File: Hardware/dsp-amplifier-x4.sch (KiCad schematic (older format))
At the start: 65 parts, among them J1 USBi, J2 EXT, J3 Raspberry_Pi_2_3, J4 Screw_Terminal_01x02, J5 Screw_Terminal_01x02, J6 Screw_Terminal_01x02, J7 Screw_Terminal_01x02, P1 Conn_WallPlug, Q1 STD2805, U1 ADAU1452, U2 TSOP583xx

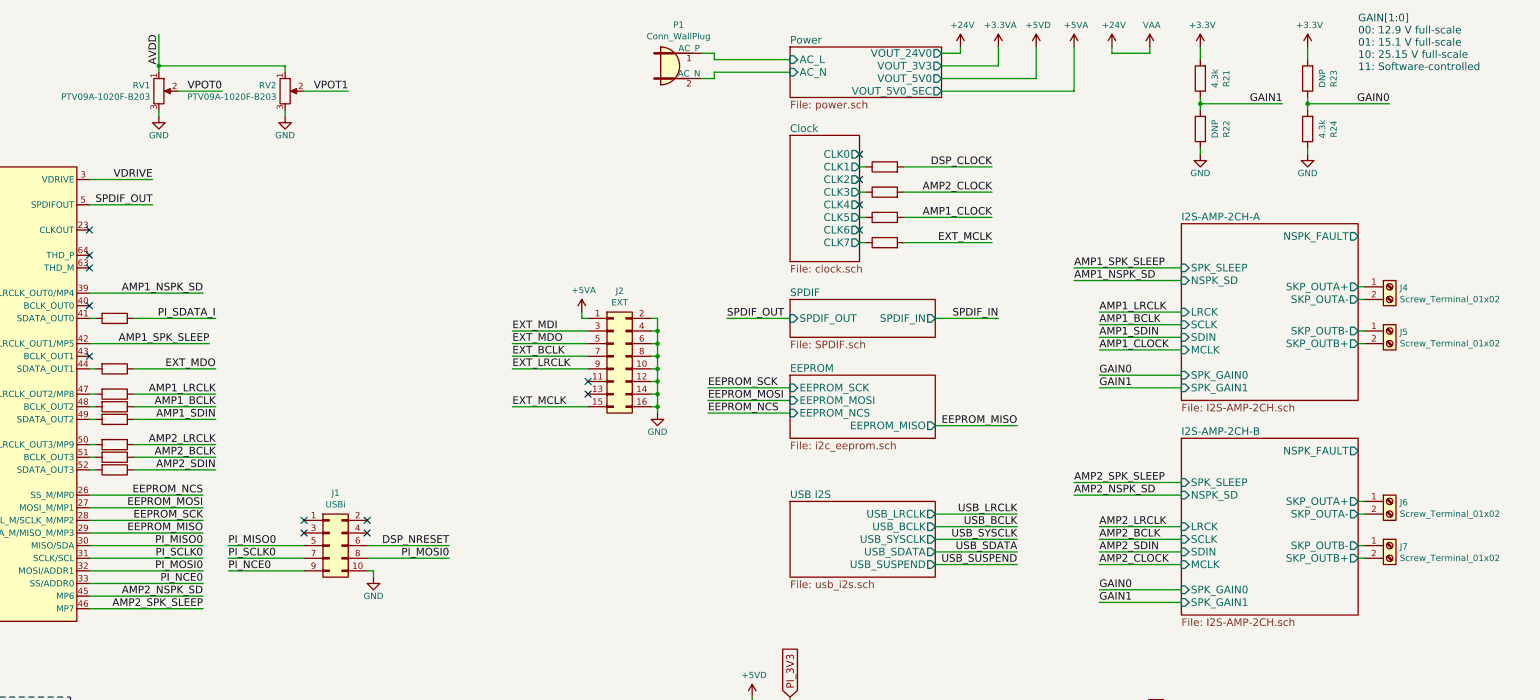
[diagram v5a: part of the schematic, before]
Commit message: software gain control
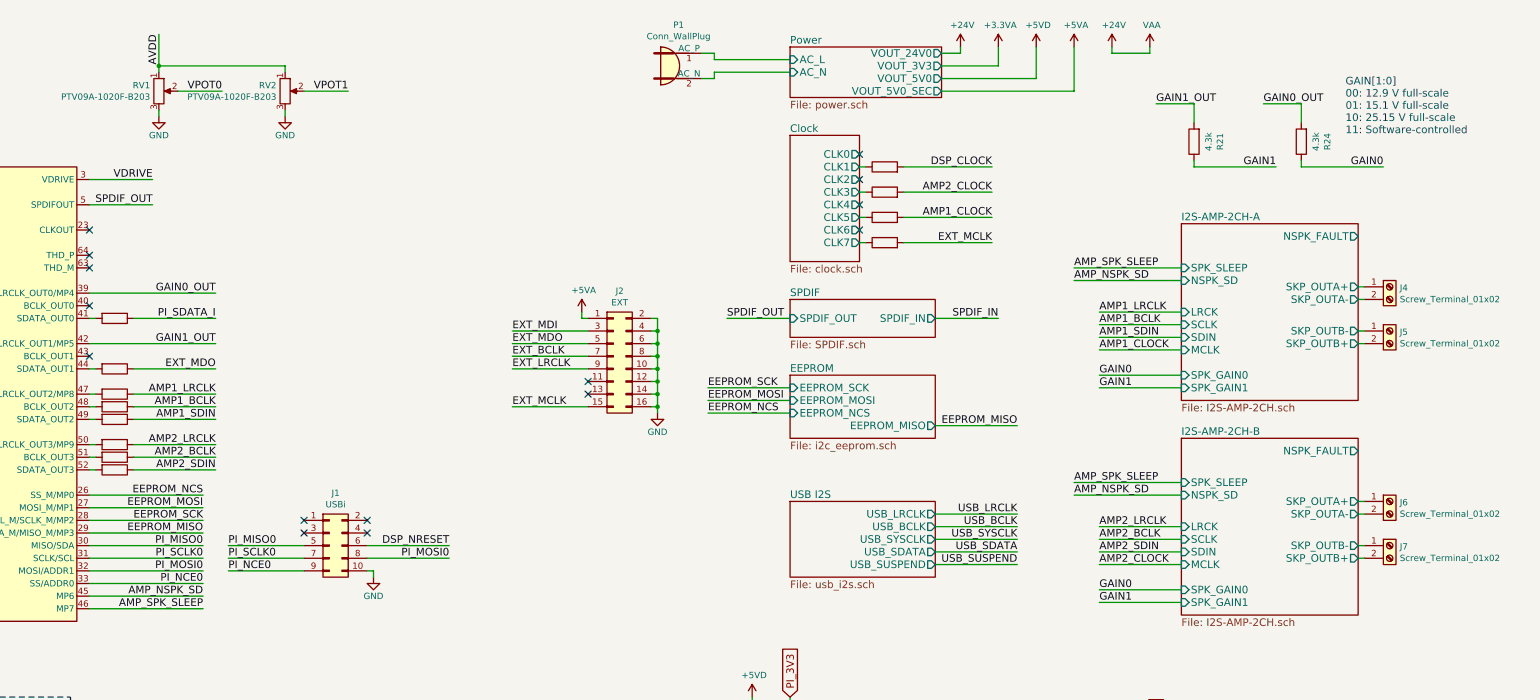
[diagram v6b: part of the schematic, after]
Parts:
- removed R22, R23: DNP, Resistor_SMD:R_0603_1608Metric_Pad0.98x0.95mm_HandSolder, symbol Device:R
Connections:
- net +3V3: no longer R21.2
- net GAIN0: now also R24.1; no longer R24.2
- net GND: no longer R24.1
- net AMP1_NSPK_SD renamed GAIN0_OUT
- net GAIN0_OUT: now also R24.2
- net AMP1_SPK_SLEEP renamed GAIN1_OUT
- net GAIN1_OUT: now also R21.2
- net AMP2_NSPK_SD renamed AMP_NSPK_SD
- net AMP2_SPK_SLEEP renamed AMP_SPK_SLEEP
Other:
- moved on the sheet: R21, R24
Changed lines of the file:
@@
 	14450 2800 14500 2800
 Text Label 12200 2750 0    60   ~ 0
-AMP1_NSPK_SD
+AMP_NSPK_SD
 Text Label 12200 2650 0    60   ~ 0
-AMP1_SPK_SLEEP
+AMP_SPK_SLEEP
 Wire Wire Line
 	12200 2650 13050 2650
 Wire Wire Line
 	13050 2750 12200 2750
-Text Label 5300 2850 2    60   ~ 0
-AMP1_NSPK_SD
-Text Label 5350 3250 2    60   ~ 0
-AMP1_SPK_SLEEP
-Wire Wire Line
-	5300 2850 4400 2850
 Text Label 5300 5250 2    60   ~ 0
-AMP2_NSPK_SD
+AMP_NSPK_SD
 Text Label 5300 5350 2    60   ~ 0
-AMP2_SPK_SLEEP
+AMP_SPK_SLEEP
 Wire Wire Line
 	4400 5350 5300 5350
@@
 Wire Wire Line
 	12400 3600 13050 3600
-Text Label 13850 1350 2    60   ~ 0
+Text Label 13800 1850 2    60   ~ 0
 GAIN1
 Wire Wire Line
-	13200 1350 13850 1350
-$Comp
-L power:+3.3V #PWR035
-U 1 1 60DB0BF6
-P 13200 900
-F 0 "#PWR035" H 13200 750 50  0001 C CNN
-F 1 "+3.3V" H 13215 1073 50  0000 C CNN
-F 2 "" H 13200 900 50  0001 C CNN
-F 3 "" H 13200 900 50  0001 C CNN
-	1    13200 900
-	1    0    0    -1
-$EndComp
-$Comp
-L power:GND #PWR036
-U 1 1 60DE0F78
-P 13200 1750
-F 0 "#PWR036" H 13200 1500 50  0001 C CNN
-F 1 "GND" H 13200 1600 50  0000 C CNN
-F 2 "" H 13200 1750 50  0001 C CNN
-F 3 "" H 13200 1750 50  0001 C CNN
-	1    13200 1750
-	1    0    0    -1
-$EndComp
-Wire Wire Line
-	13200 1700 13200 1750
+	13150 1850 13800 1850
 $Comp
 L Device:R R21
 U 1 1 60E78271
-P 13200 1150
-F 0 "R21" V 12993 1150 50  0000 C CNN
-F 1 "4.3k" V 13084 1150 50  0000 C CNN
-F 2 "Resistor_SMD:R_0603_1608Metric_Pad0.98x0.95mm_HandSolder" V 13130 1150 50  0001 C CNN
-F 3 "~" H 13200 1150 50  0001 C CNN
-	1    13200 1150
+P 13150 1650
+F 0 "R21" V 12943 1650 50  0000 C CNN
+F 1 "4.3k" V 13034 1650 50  0000 C CNN
+F 2 "Resistor_SMD:R_0603_1608Metric_Pad0.98x0.95mm_HandSolder" V 13080 1650 50  0001 C CNN
+F 3 "~" H 13150 1650 50  0001 C CNN
+	1    13150 1650
 	-1   0    0    1
 $EndComp
 Wire Wire Line
-	13200 1300 13200 1350
-Wire Wire Line
-	13200 900  13200 1000
-$Comp
-L Device:R R22
-U 1 1 60F40166
-P 13200 1550
-F 0 "R22" V 12993 1550 50  0000 C CNN
-F 1 "DNP" V 13084 1550 50  0000 C CNN
-F 2 "Resistor_SMD:R_0603_1608Metric_Pad0.98x0.95mm_HandSolder" V 13130 1550 50  0001 C CNN
-F 3 "~" H 13200 1550 50  0001 C CNN
-	1    13200 1550
-	-1   0    0    1
-$EndComp
-Wire Wire Line
-	13200 1400 13200 1350
-Connection ~ 13200 1350
-Text Label 14700 1350 2    60   ~ 0
+	13150 1800 13150 1850
+Text Label 14650 1850 2    60   ~ 0
 GAIN0
 Wire Wire Line
-	14050 1350 14700 1350
-$Comp
-L power:+3.3V #PWR037
-U 1 1 60FBEEDA
-P 14050 900
-F 0 "#PWR037" H 14050 750 50  0001 C CNN
-F 1 "+3.3V" H 14065 1073 50  0000 C CNN
-F 2 "" H 14050 900 50  0001 C CNN
-F 3 "" H 14050 900 50  0001 C CNN
-	1    14050 900
-	1    0    0    -1
-$EndComp
-$Comp
-L power:GND #PWR038
-U 1 1 60FBEEE0
-P 14050 1750
-F 0 "#PWR038" H 14050 1500 50  0001 C CNN
-F 1 "GND" H 14050 1600 50  0000 C CNN
-F 2 "" H 14050 1750 50  0001 C CNN
-F 3 "" H 14050 1750 50  0001 C CNN
-	1    14050 1750
-	1    0    0    -1
-$EndComp
-Wire Wire Line
-	14050 1700 14050 1750
+	14000 1850 14650 1850
 $Comp
 L Device:R R24
 U 1 1 60FBEEE7
-P 14050 1550
-F 0 "R24" V 13843 1550 50  0000 C CNN
-F 1 "4.3k" V 13934 1550 50  0000 C CNN
-F 2 "Resistor_SMD:R_0603_1608Metric_Pad0.98x0.95mm_HandSolder" V 13980 1550 50  0001 C CNN
-F 3 "~" H 14050 1550 50  0001 C CNN
-	1    14050 1550
+P 14000 1650
+F 0 "R24" V 13793 1650 50  0000 C CNN
+F 1 "4.3k" V 13884 1650 50  0000 C CNN
+F 2 "Resistor_SMD:R_0603_1608Metric_Pad0.98x0.95mm_HandSolder" V 13930 1650 50  0001 C CNN
+F 3 "~" H 14000 1650 50  0001 C CNN
+	1    14000 1650
 	-1   0    0    1
 $EndComp
-Wire Wire Line
-	14050 1300 14050 1350
-Wire Wire Line
-	14050 900  14050 1000
-$Comp
-L Device:R R23
-U 1 1 60FBEEEF
-P 14050 1150
-F 0 "R23" V 13843 1150 50  0000 C CNN
-F 1 "DNP" V 13934 1150 50  0000 C CNN
-F 2 "Resistor_SMD:R_0603_1608Metric_Pad0.98x0.95mm_HandSolder" V 13980 1150 50  0001 C CNN
-F 3 "~" H 14050 1150 50  0001 C CNN
-	1    14050 1150
-	-1   0    0    1
-$EndComp
-Wire Wire Line
-	14050 1400 14050 1350
-Connection ~ 14050 1350
 $Sheet
 S 13050 4000 1400 1400
@@
 	12400 5000 13050 5000
 Text Label 12200 4450 0    60   ~ 0
-AMP2_NSPK_SD
+AMP_NSPK_SD
 Text Label 12200 4350 0    60   ~ 0
-AMP2_SPK_SLEEP
+AMP_SPK_SLEEP
 Wire Wire Line
 	12200 4350 13050 4350
@@
 NoConn ~ 10500 2150
 NoConn ~ 10500 2350
-Text Notes 14450 1100 0    60   ~ 0
+Text Notes 14350 1600 0    60   ~ 0
 GAIN[1:0]\n00: 12.9 V full-scale\n01: 15.1 V full-scale\n10: 25.15 V full-scale\n11: Software-controlled
 Wire Wire Line
@@
 Wire Wire Line
 	4400 4450 5300 4450
-Wire Wire Line
-	4400 3250 5350 3250
 $Comp
 L Device:R R2
@@
 Text Label 4950 800  3    60   ~ 0
 AVDD
+Wire Wire Line
+	14000 1800 14000 1850
+Text Label 13700 1350 0    60   ~ 0
+GAIN0_OUT
+Text Label 12850 1350 0    60   ~ 0
+GAIN1_OUT
+Wire Wire Line
+	12850 1350 13150 1350
+Wire Wire Line
+	13150 1350 13150 1500
+Wire Wire Line
+	13700 1350 14000 1350
+Wire Wire Line
+	14000 1350 14000 1500
+Text Label 5400 2850 2    60   ~ 0
+GAIN0_OUT
+Text Label 5400 3250 2    60   ~ 0
+GAIN1_OUT
+Wire Wire Line
+	5400 3250 4400 3250
+Wire Wire Line
+	4400 2850 5400 2850
 $EndSCHEMATC
